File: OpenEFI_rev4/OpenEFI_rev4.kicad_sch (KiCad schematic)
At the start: 92 parts, among them J1 USB_B, J2 Tag connect, J4 Conn_02x08_Odd_Even, J7 Conn_01x04, J8 Micro_SD_Card_Det1, Q1 AO3400A, Q11 SS8050, Q12 AO3400A, Q13 AO3400A, Q2 AO3400A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

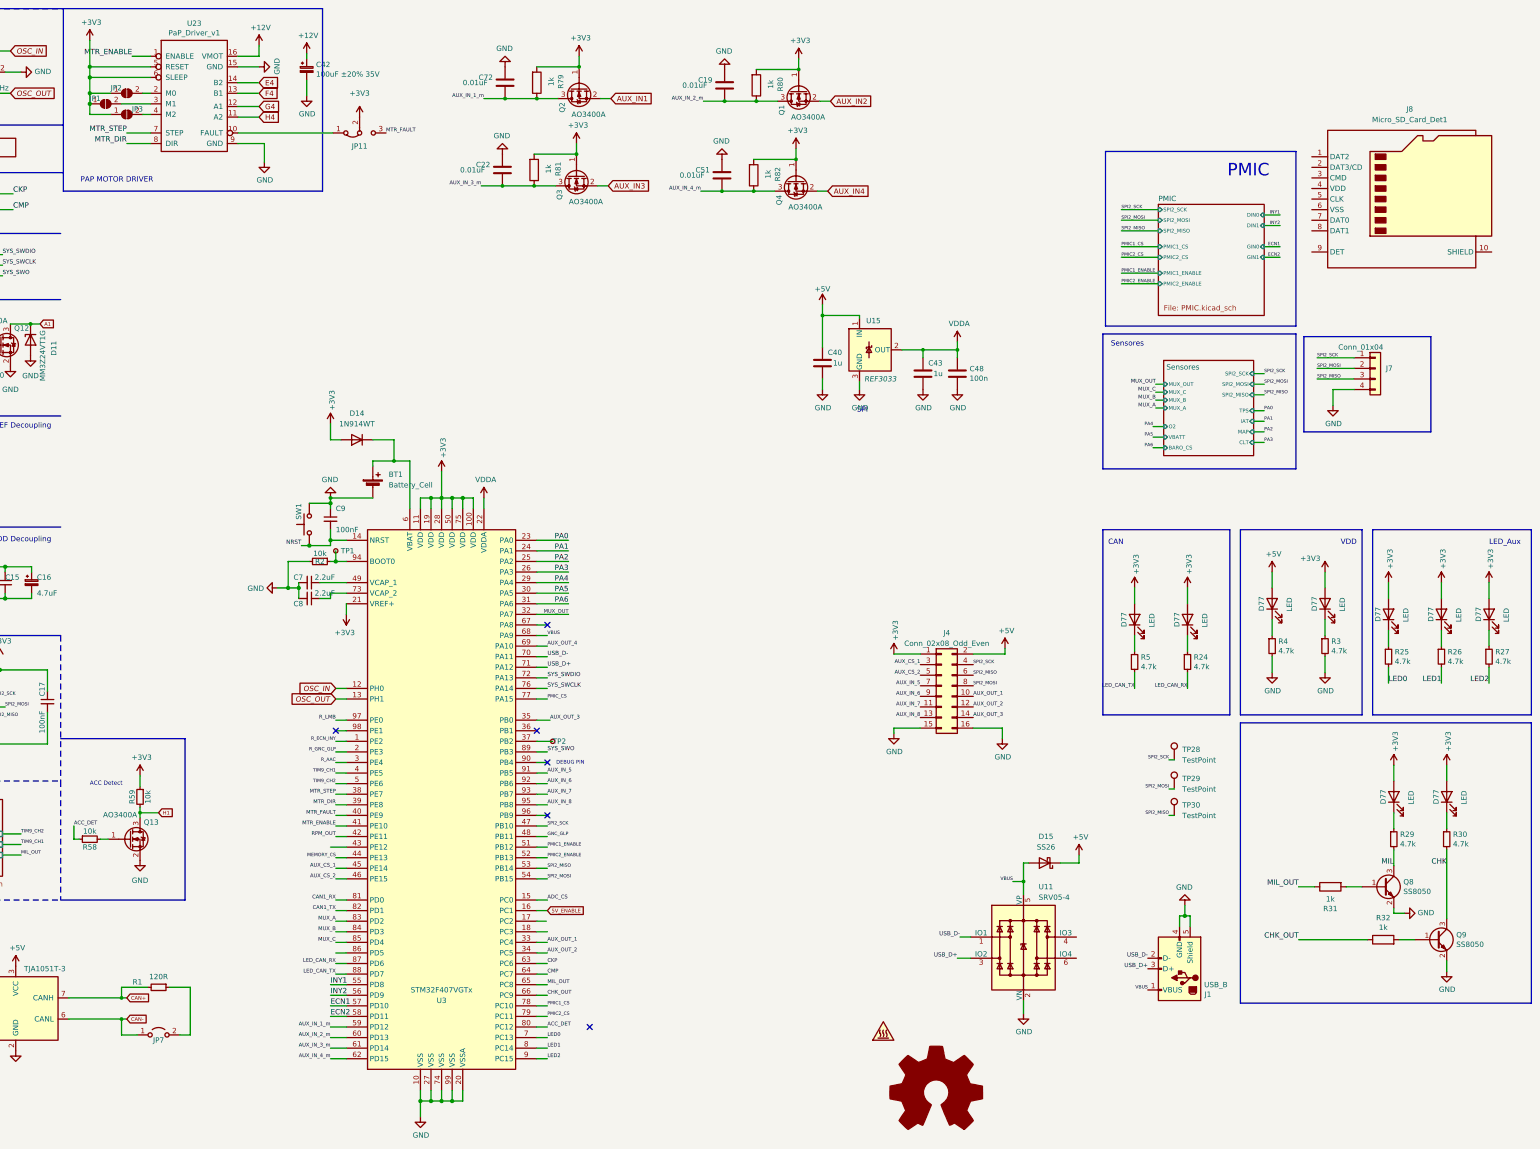
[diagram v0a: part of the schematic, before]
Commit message: update sensors/connector pinout, added rtc vbatt backup
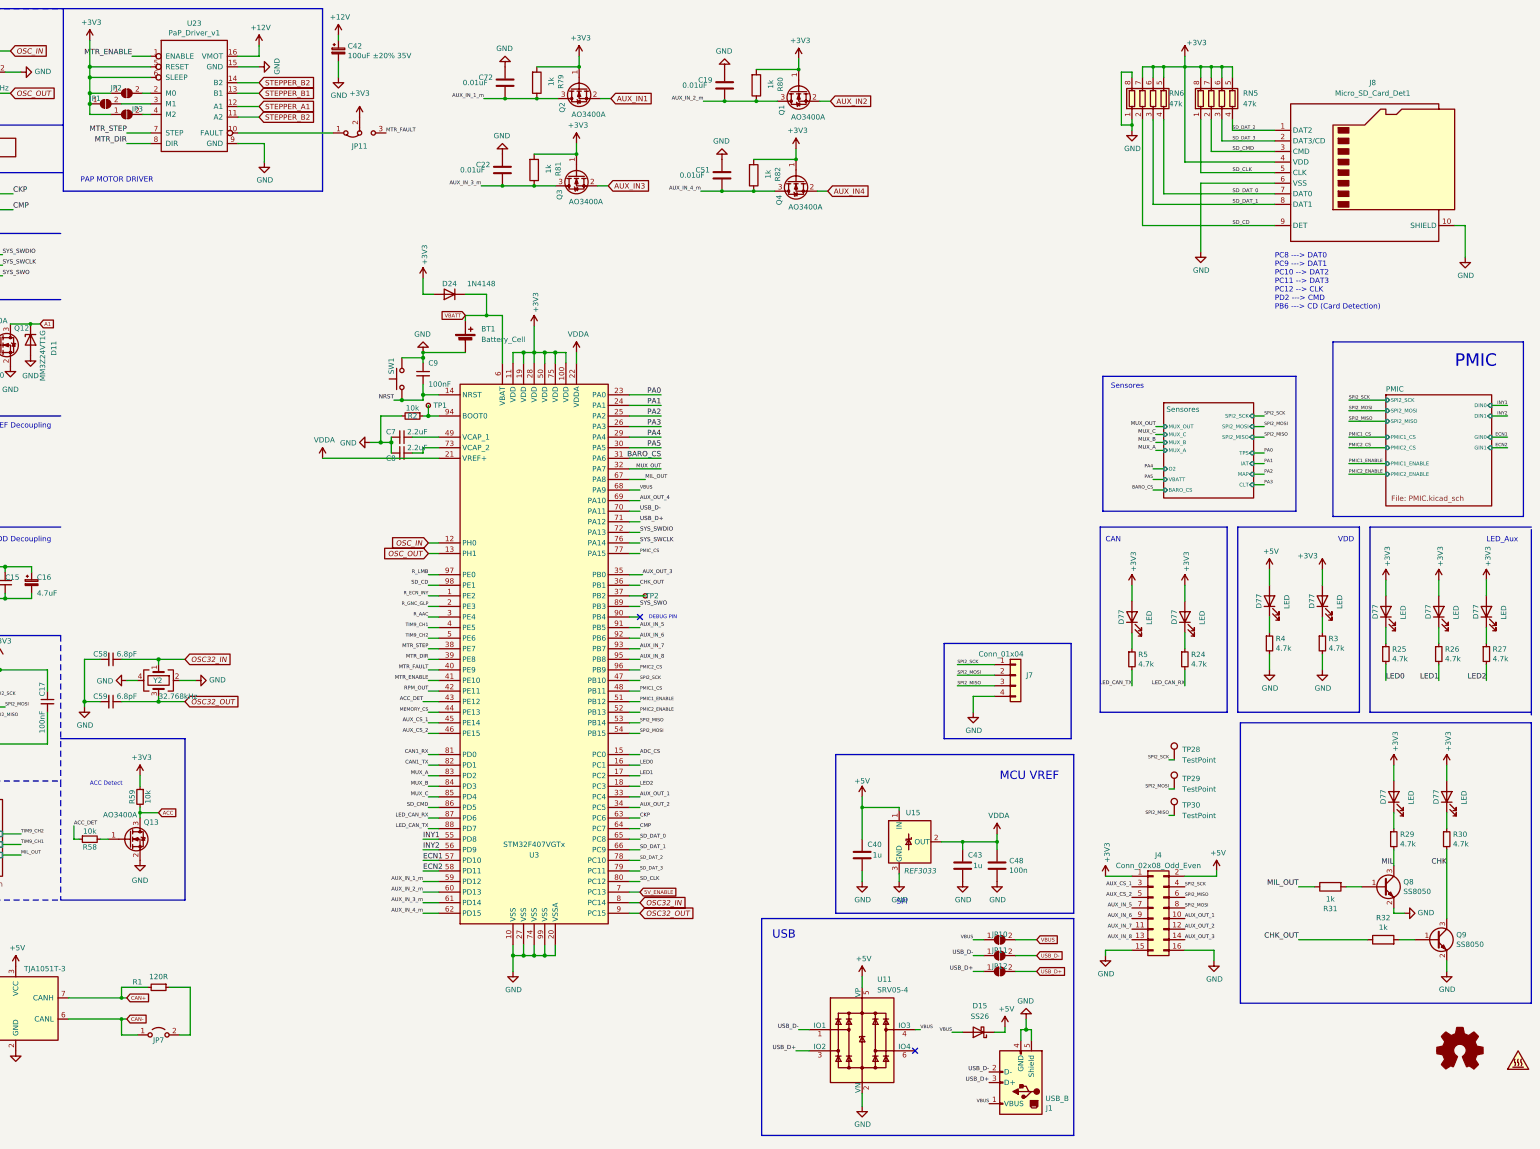
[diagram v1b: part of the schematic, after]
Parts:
- removed D14: 1N914WT, Diode_SMD:D_SOD-523, symbol Diode:1N914WT
- added C58, C59: 6.8pF, Capacitor_SMD:C_0805_2012Metric, symbol Device:C_Small
- added D24: 1N4148, Diode_SMD:D_SOD-523, symbol Diode:1N4148
- added JP10, JP11, JP12: SolderJumper_2_Open, Jumper:SolderJumper-2_P1.3mm_Open_Pad1.0x1.5mm, symbol Jumper:SolderJumper_2_Open
- added RN5, RN6: 47k, Resistor_SMD:R_Array_Convex_4x0603, symbol Device:R_Pack04
- added Y2: 32.768kHz, Crystal:Crystal_SMD_2012-2Pin_2.0x1.2mm, symbol Device:Crystal_GND24
- LOGO1: symbol Graphic:Logo_Open_Hardware_Large -> Graphic:Logo_Open_Hardware_Small; now left out of the parts list
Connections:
- net GNC_GLP is gone; now on net PMIC1_CS: U3.48 (PB11)
- net H4 is gone; now on net STEPPER_B2: U23.11 (A2)
- net +3V3: now also J8.4 (VDD), D24.2 (A), RN5.5 (R4.2), RN5.6 (R3.2), RN5.7 (R2.2), RN5.8 (R1.2), RN6.5 (R4.2), RN6.6 (R3.2), RN6.7 (R2.2); no longer U3.21 (VREF+)
- net +5V: now also U11.5 (VP)
- net 5V_ENABLE: now also U3.7 (PC13); no longer U3.16 (PC1)
- net ACC_DET: now also U3.43 (PE12); no longer U3.80 (PC12)
- net CHK_OUT: now also U3.36 (PB1); no longer U3.66 (PC9)
- net GND: now also J8.10 (SHIELD), J8.6 (VSS), C58.2, C59.2, RN6.1 (R1.1), RN6.8 (R1.2), Y2.2, Y2.4
- net LED0: now also U3.16 (PC1); no longer U3.7 (PC13)
- net LED1: now also U3.17 (PC2); no longer U3.8 (PC14)
- net LED2: now also U3.18 (PC3); no longer U3.9 (PC15)
- net MIL_OUT: now also U3.67 (PA8); no longer U3.65 (PC8)
- net PMIC1_CS: no longer U3.78 (PC10)
- net PMIC2_CS: now also U3.96 (PB9); no longer U3.79 (PC11)
- net USB_D+: now also JP12.1 (A), JP12.2 (B)
- net USB_D-: now also JP11.1 (A), JP11.2 (B)
- net VBUS: now also U11.4 (IO3), JP10.1 (A), JP10.2 (B); no longer U11.5 (VP)
- net VDDA: now also U3.21 (VREF+)
- net VBATT: now reaches BT1.1 (+), U3.6 (VBAT)
- net VBATT: now also D24.1 (K)
- net SD_CMD: now reaches U3.86 (PD5)
- net SD_CMD: now also J8.3 (CMD), RN5.2 (R2.1)
- net SD_CD: now reaches U3.98 (PE1)
- net SD_CD: now also J8.9 (DET), RN6.2 (R2.1)
- net SD_DAT_2: now reaches J8.1 (DAT2)
- net SD_DAT_2: now also U3.78 (PC10), RN5.4 (R4.1)
- net SD_DAT_3: now reaches J8.2 (DAT3/CD)
- net SD_DAT_3: now also U3.79 (PC11), RN5.3 (R3.1)
- net SD_CLK: now reaches J8.5 (CLK)
- net SD_CLK: now also U3.80 (PC12), RN5.1 (R1.1)
- net SD_DAT_0: now reaches J8.7 (DAT0)
- net SD_DAT_0: now also U3.65 (PC8), RN6.4 (R4.1)
- net SD_DAT_1: now reaches J8.8 (DAT1)
- net SD_DAT_1: now also U3.66 (PC9), RN6.3 (R3.1)
- net E4 renamed STEPPER_B2
- net F4 renamed STEPPER_B1
- net G4 renamed STEPPER_A1
- net H1 renamed ACC
- net PA6 renamed BARO_CS
- new net OSC32_IN: C58.1, U3.8 (PC14), Y2.1
- new net OSC32_OUT: C59.1, U3.9 (PC15), Y2.3
- no-connect marks 6 -> 2
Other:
- note added: "MCU VREF"
- note added: "PC8 ---> DAT0 PC9 ---> DAT1 PC10 --> DAT2 PC11 --> DAT3 PC12 --> CLK PD2 ---> CMD PB6 ---> CD (Card Detection)"
- note added: "USB"
- moved on the sheet: BT1, C40, C42, C43, C48, C7, C8, C9, D15, D77, J1, J4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

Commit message: WIP Analog frontend
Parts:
- removed Q13: AO3400A, Package_TO_SOT_SMD:SOT-23, symbol Transistor_FET:AO3400A
- removed R58: 10k, Resistor_SMD:R_0805_2012Metric, symbol Device:R_Small
- removed R59: 10k, Resistor_SMD:R_0603_1608Metric, symbol Device:R_Small
- removed Y2: 32.768kHz, Crystal:Crystal_SMD_2012-2Pin_2.0x1.2mm, symbol Device:Crystal_GND24
- added C31: 0.01uF, Capacitor_SMD:C_0805_2012Metric, symbol Device:C
- added Q19: AO3400A, Package_TO_SOT_SMD:SOT-23, symbol Transistor_FET:AO3400A
- added R85: 1k, Resistor_SMD:R_0603_1608Metric, symbol Device:R
- added TP23: TestPoint_Alt, TestPoint:TestPoint_THTPad_1.0x1.0mm_Drill0.5mm, symbol Connector:TestPoint_Alt
- added Y3: 32.768kHz, Crystal:Crystal_SMD_2012-2Pin_2.0x1.2mm, symbol Device:Crystal
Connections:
- net +3V3: now also Q19.1 (G), R85.2
- net ACC: now also Q19.2 (S)
- net ACC_DET: now also C31.2, Q19.3 (D), R85.1, TP23.1
- net GND: now also C31.1
- net OSC32_IN: now also Y3.2
- net OSC32_OUT: now also Y3.1

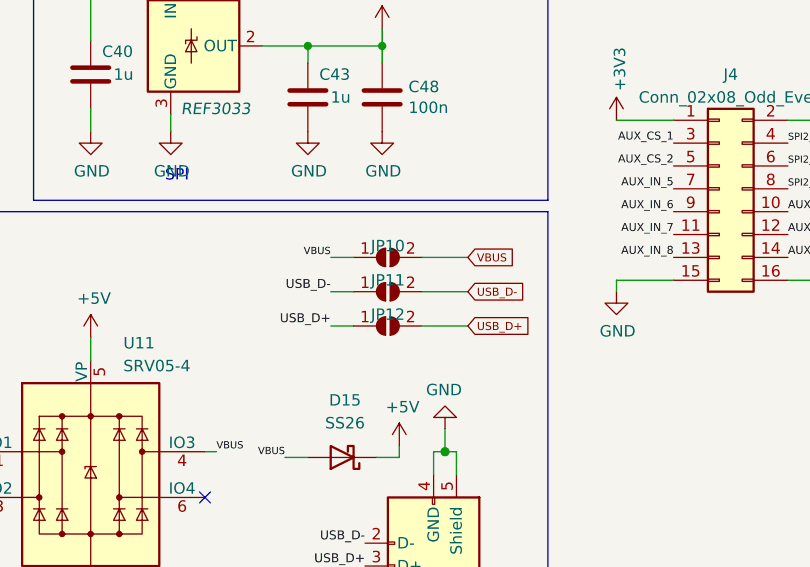
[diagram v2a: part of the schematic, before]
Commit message: WIP analog frontend, init ckp"
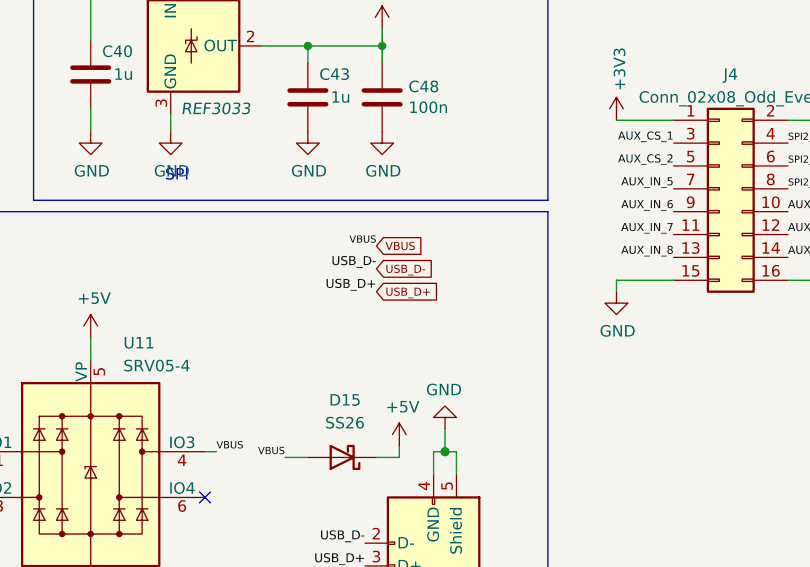
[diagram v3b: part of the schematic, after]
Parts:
- removed JP10, JP11, JP12: SolderJumper_2_Open, Jumper:SolderJumper-2_P1.3mm_Open_Pad1.0x1.5mm, symbol Jumper:SolderJumper_2_Open
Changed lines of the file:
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@@
     (stroke (width 0) (type default))
   )
-  (wire (pts (xy 283.21 240.03) (xy 288.29 240.03))
-    (stroke (width 0) (type default))
-  )
   (polyline (pts (xy 336.55 181.61) (xy 365.76 181.61))
     (stroke (width 0.152) (type solid))
@@
     (stroke (width 0) (type solid))
   )
-  (wire (pts (xy 273.05 243.84) (xy 275.59 243.84))
-    (stroke (width 0) (type default))
-  )
   (wire (pts (xy 26.67 22.86) (xy 35.56 22.86))
     (stroke (width 0) (type solid))
@@
     (stroke (width 0) (type default))
   )
-  (wire (pts (xy 283.21 243.84) (xy 288.29 243.84))
-    (stroke (width 0) (type default))
-  )
   (wire (pts (xy 133.35 116.84) (xy 133.35 119.38))
     (stroke (width 0) (type solid))
@@
     (stroke (width 0) (type solid))
   )
-  (wire (pts (xy 283.21 236.22) (xy 288.29 236.22))
-    (stroke (width 0) (type default))
-  )
   (wire (pts (xy 374.015 228.6) (xy 374.015 229.87))
     (stroke (width 0) (type solid))
@@
     (stroke (width 0) (type default))
   )
-  (wire (pts (xy 273.05 240.03) (xy 275.59 240.03))
-    (stroke (width 0) (type default))
-  )
   (wire (pts (xy 344.17 147.32) (xy 344.17 151.13))
     (stroke (width 0) (type solid))
@@
     (stroke (width 0) (type solid))
   )
-  (wire (pts (xy 273.05 236.22) (xy 275.59 236.22))
-    (stroke (width 0) (type default))
-  )
   (wire (pts (xy 35.56 153.035) (xy 35.56 154.305))
     (stroke (width 0) (type solid))
@@
     (effects (font (size 0.889 0.889)) (justify right bottom))
   )
+  (label "USB_D+" (at 278.13 240.03 180) (fields_autoplaced)
+    (effects (font (size 0.9906 0.9906)) (justify right bottom))
+  )
   (label "AUX_CS_2" (at 311.15 226.06 180) (fields_autoplaced)
     (effects (font (size 0.889 0.889)) (justify right bottom))
@@
     (effects (font (size 0.7874 0.7874)) (justify left bottom))
   )
+  (label "VBUS" (at 278.13 234.95 180) (fields_autoplaced)
+    (effects (font (size 0.8 0.8)) (justify right bottom))
+  )
   (label "MEMORY_CS" (at 142.24 181.61 180) (fields_autoplaced)
     (effects (font (size 0.8 0.8)) (justify right bottom))
@@
     (effects (font (size 1.27 1.27)) (justify right bottom))
   )
-  (label "USB_D+" (at 273.05 243.84 180) (fields_autoplaced)
-    (effects (font (size 0.9906 0.9906)) (justify right bottom))
-  )
   (label "ECN1" (at 140.97 217.17 0) (fields_autoplaced)
     (effects (font (size 1.27 1.27)) (justify left bottom))
@@
     (effects (font (size 1.27 1.27)) (justify right bottom))
   )
-  (label "USB_D-" (at 273.05 240.03 180) (fields_autoplaced)
-    (effects (font (size 0.9906 0.9906)) (justify right bottom))
-  )
   (label "MIL_OUT" (at 351.155 223.52 180) (fields_autoplaced)
     (effects (font (size 1.27 1.27)) (justify right bottom))
@@
     (effects (font (size 1.27 1.27)) (justify right bottom))
   )
+  (label "USB_D-" (at 278.13 237.49 180) (fields_autoplaced)
+    (effects (font (size 0.9906 0.9906)) (justify right bottom))
+  )
   (label "SD_DAT_0" (at 193.04 212.09 0) (fields_autoplaced)
     (effects (font (size 0.889 0.889)) (justify left bottom))
@@
     (effects (font (size 0.889 0.889)) (justify left bottom))
   )
-  (label "VBUS" (at 273.05 236.22 180) (fields_autoplaced)
-    (effects (font (size 0.8 0.8)) (justify right bottom))
-  )
   (label "AUX_IN_4_m" (at 140.97 229.87 180) (fields_autoplaced)
     (effects (font (size 0.889 0.889)) (justify right bottom))
@@
     )
   )
-  (global_label "USB_D-" (shape input) (at 288.29 240.03 0) (fields_autoplaced)
-    (effects (font (size 0.889 0.889)) (justify left))
-    (property "Intersheetrefs" "${INTERSHEET_REFS}" (at 295.78 240.03 0)
-      (effects (font (size 1.27 1.27)) (justify left) hide)
-    )
-  )
   (global_label "OSC_OUT" (shape input) (at 41.91 33.02 0) (fields_autoplaced)
     (effects (font (size 1.27 1.27) italic) (justify left))
@@
     )
   )
-  (global_label "VBUS" (shape input) (at 288.29 236.22 0) (fields_autoplaced)
-    (effects (font (size 0.889 0.889)) (justify left))
-    (property "Intersheetrefs" "${INTERSHEET_REFS}" (at 293.875 236.22 0)
-      (effects (font (size 1.27 1.27)) (justify left) hide)
-    )
-  )
   (global_label "CAN+" (shape input) (at 69.85 250.19 0)
     (effects (font (size 0.889 0.889)) (justify left))
@@
     )
   )
-  (global_label "USB_D+" (shape input) (at 288.29 243.84 0) (fields_autoplaced)
+  (global_label "USB_D+" (shape input) (at 278.13 240.03 0) (fields_autoplaced)
     (effects (font (size 0.889 0.889)) (justify left))
-    (property "Intersheetrefs" "${INTERSHEET_REFS}" (at 295.78 243.84 0)
+    (property "Intersheetrefs" "${INTERSHEET_REFS}" (at 285.62 240.03 0)
       (effects (font (size 1.27 1.27)) (justify left) hide)
     )
@@
     )
   )
+  (global_label "USB_D-" (shape input) (at 278.13 237.49 0) (fields_autoplaced)
+    (effects (font (size 0.889 0.889)) (justify left))
+    (property "Intersheetrefs" "${INTERSHEET_REFS}" (at 285.62 237.49 0)
+      (effects (font (size 1.27 1.27)) (justify left) hide)
+    )
+  )
   (global_label "OSC_IN" (shape input) (at 142.24 140.97 180)
     (effects (font (size 1.27 1.27) italic) (justify right))
@@
     )
   )
+  (global_label "VBUS" (shape input) (at 278.13 234.95 0) (fields_autoplaced)
+    (effects (font (size 0.889 0.889)) (justify left))
+    (property "Intersheetrefs" "${INTERSHEET_REFS}" (at 283.715 234.95 0)
+      (effects (font (size 1.27 1.27)) (justify left) hide)
+    )
+  )
   (global_label "STEPPER_B2" (shape input) (at 101.6 38.735 0)
     (effects (font (size 1.27 1.27)) (justify left))
@@
     )
   )
-  (symbol (lib_id "Jumper:SolderJumper_2_Open") (at 279.4 240.03 0) (unit 1)
-    (in_bom yes) (on_board yes) (dnp no)
-    (property "Reference" "JP11" (at 279.4 238.76 0)
-      (effects (font (size 1.27 1.27)))
-    )
-    (property "Value" "SolderJumper_2_Open" (at 279.4 236.22 0)
-      (effects (font (size 1.27 1.27)) hide)
-    )
-    (property "Footprint" "Jumper:SolderJumper-2_P1.3mm_Open_Pad1.0x1.5mm" (at 279.4 240.03 0)
-      (effects (font (size 1.27 1.27)) hide)
-    )
-    (property "Datasheet" "~" (at 279.4 240.03 0)
-      (effects (font (size 1.27 1.27)) hide)
-    )
-    (pin "1")
-    (pin "2")
-    (instances
-      (project "OpenEFI_rev4"
-        (path "/b282ce4b-c3d0-4c94-b06c-73b92bb672a9"
-          (reference "JP11") (unit 1)
-        )
-      )
-    )
-  )
   (symbol (lib_id "Connector:TestPoint") (at 321.31 193.04 0) (unit 1)
     (in_bom yes) (on_board yes) (dnp no)
@@
     )
   )
-  (symbol (lib_id "Jumper:SolderJumper_2_Open") (at 279.4 243.84 0) (unit 1)
-    (in_bom yes) (on_board yes) (dnp no)
-    (property "Reference" "JP12" (at 279.4 242.57 0)
-      (effects (font (size 1.27 1.27)))
-    )
-    (property "Value" "SolderJumper_2_Open" (at 279.4 240.03 0)
-      (effects (font (size 1.27 1.27)) hide)
-    )
-    (property "Footprint" "Jumper:SolderJumper-2_P1.3mm_Open_Pad1.0x1.5mm" (at 279.4 243.84 0)
-      (effects (font (size 1.27 1.27)) hide)
-    )
-    (property "Datasheet" "~" (at 279.4 243.84 0)
-      (effects (font (size 1.27 1.27)) hide)
-    )
-    (pin "1")
-    (pin "2")
-    (instances
-      (project "OpenEFI_rev4"
-        (path "/b282ce4b-c3d0-4c94-b06c-73b92bb672a9"
-          (reference "JP12") (unit 1)
-        )
-      )
-    )
-  )
   (symbol (lib_id "Transistor_FET:AO3400A") (at 198.12 271.78 90) (mirror x) (unit 1)
     (in_bom yes) (on_board yes) (dnp no)
@@
         )
       )
-    )
-  )
-  (symbol (lib_id "Jumper:SolderJumper_2_Open") (at 279.4 236.22 0) (unit 1)
-    (in_bom yes) (on_board yes) (dnp no)
-    (property "Reference" "JP10" (at 279.4 234.95 0)
-      (effects (font (size 1.27 1.27)))
-    )
-    (property "Value" "SolderJumper_2_Open" (at 279.4 232.41 0)
-      (effects (font (size 1.27 1.27)) hide)
-    )
-    (property "Footprint" "Jumper:SolderJumper-2_P1.3mm_Open_Pad1.0x1.5mm" (at 279.4 236.22 0)
-      (effects (font (size 1.27 1.27)) hide)
-    )
-    (property "Datasheet" "~" (at 279.4 236.22 0)
-      (effects (font (size 1.27 1.27)) hide)
-    )
-    (pin "1")
-    (pin "2")
-    (instances
-      (project "OpenEFI_rev4"
-        (path "/b282ce4b-c3d0-4c94-b06c-73b92bb672a9"
-          (reference "JP10") (unit 1)
-        )
-      )
